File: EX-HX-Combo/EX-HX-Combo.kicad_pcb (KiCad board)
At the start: 2 copper layers, 150.2 x 124.5 mm, 40 parts, among them CN1 DB9 Male, J1 IDE_CONNECTOR, J200 Bus_Tandy_Plus_Through, J3 Bus_Tandy_Plus, SW1 SW_DIP_x10, U1 BIOS FLASH, U2 74HCT245, U3 1.8432 MHz, U4 DS1315, U5 AS6C4008-55PCN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

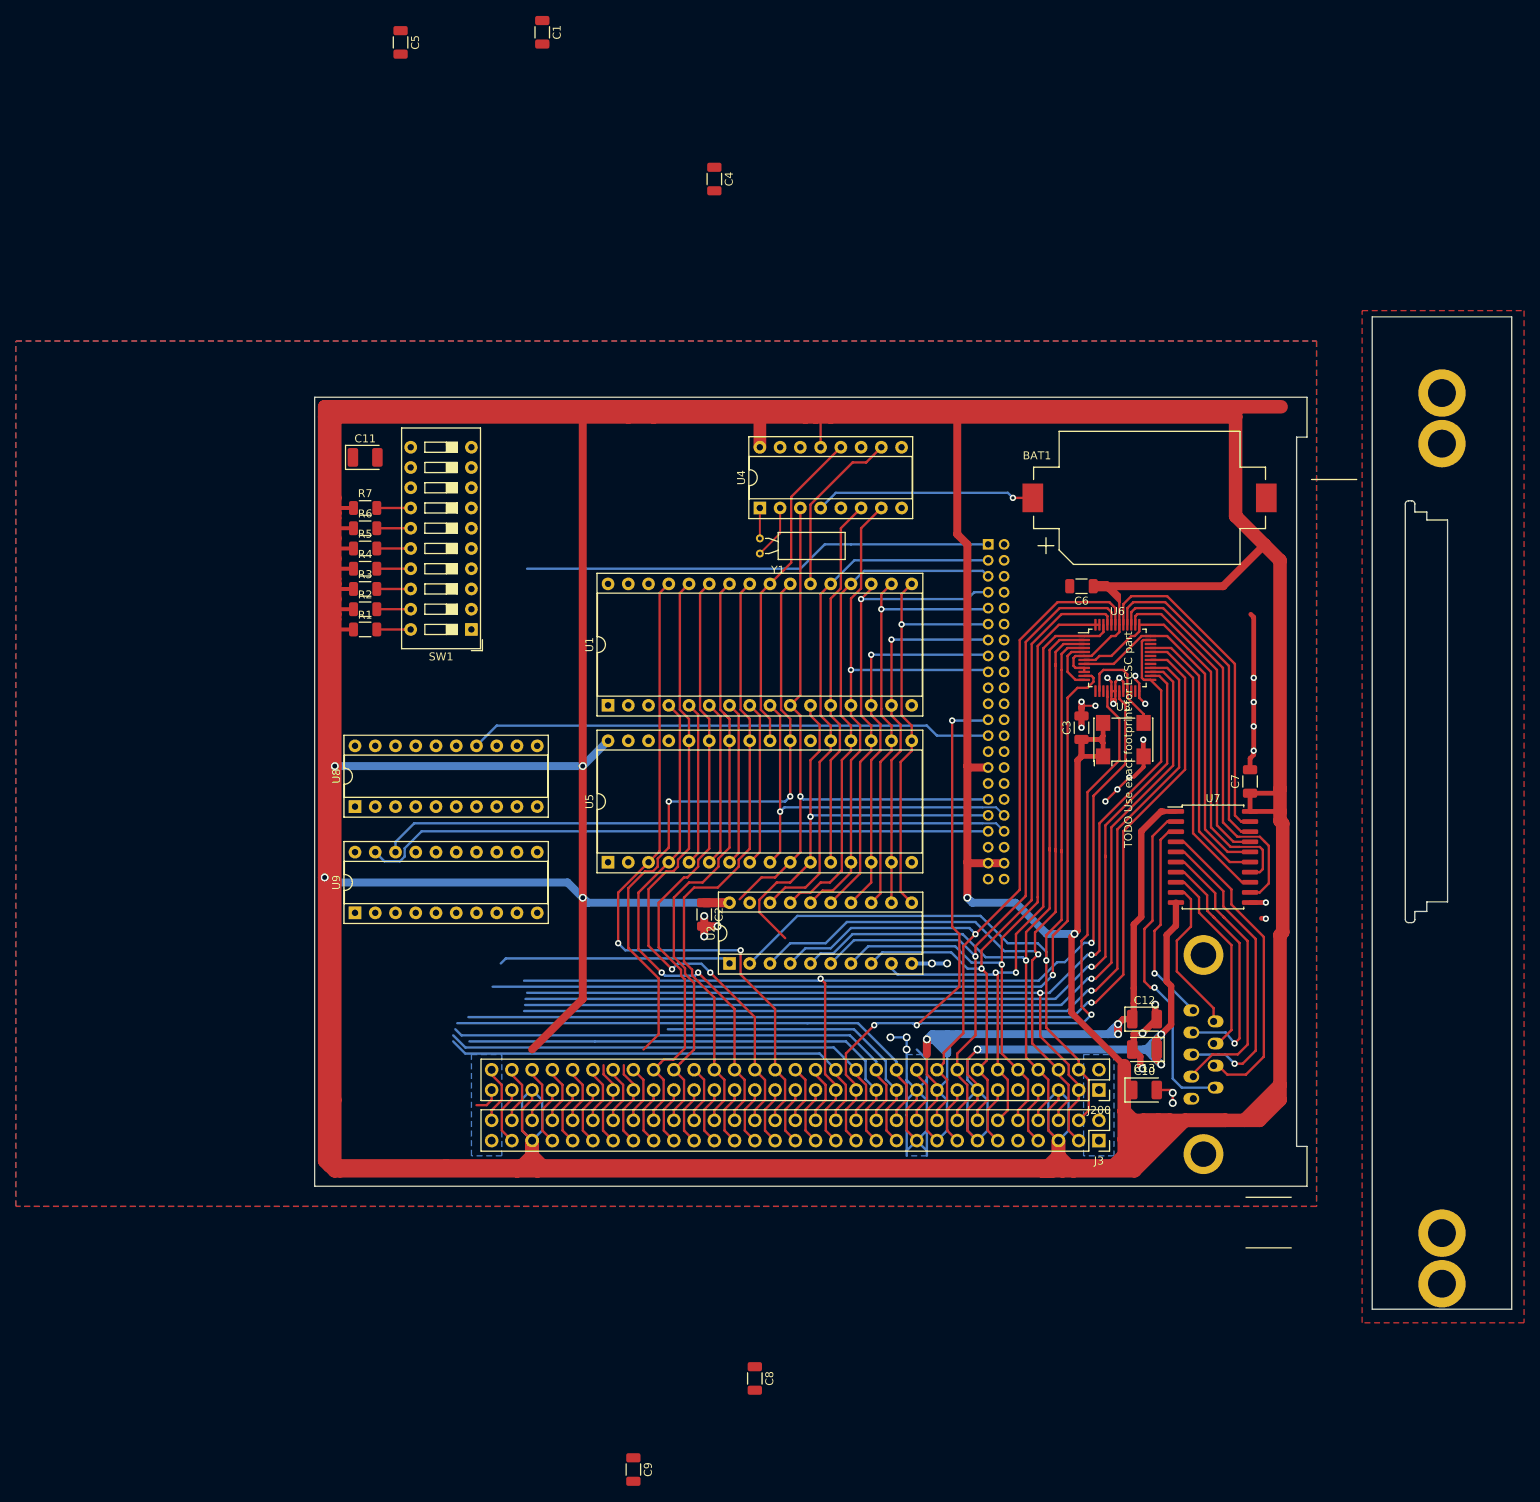
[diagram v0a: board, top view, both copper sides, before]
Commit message: More layout work on EX-HX combo.
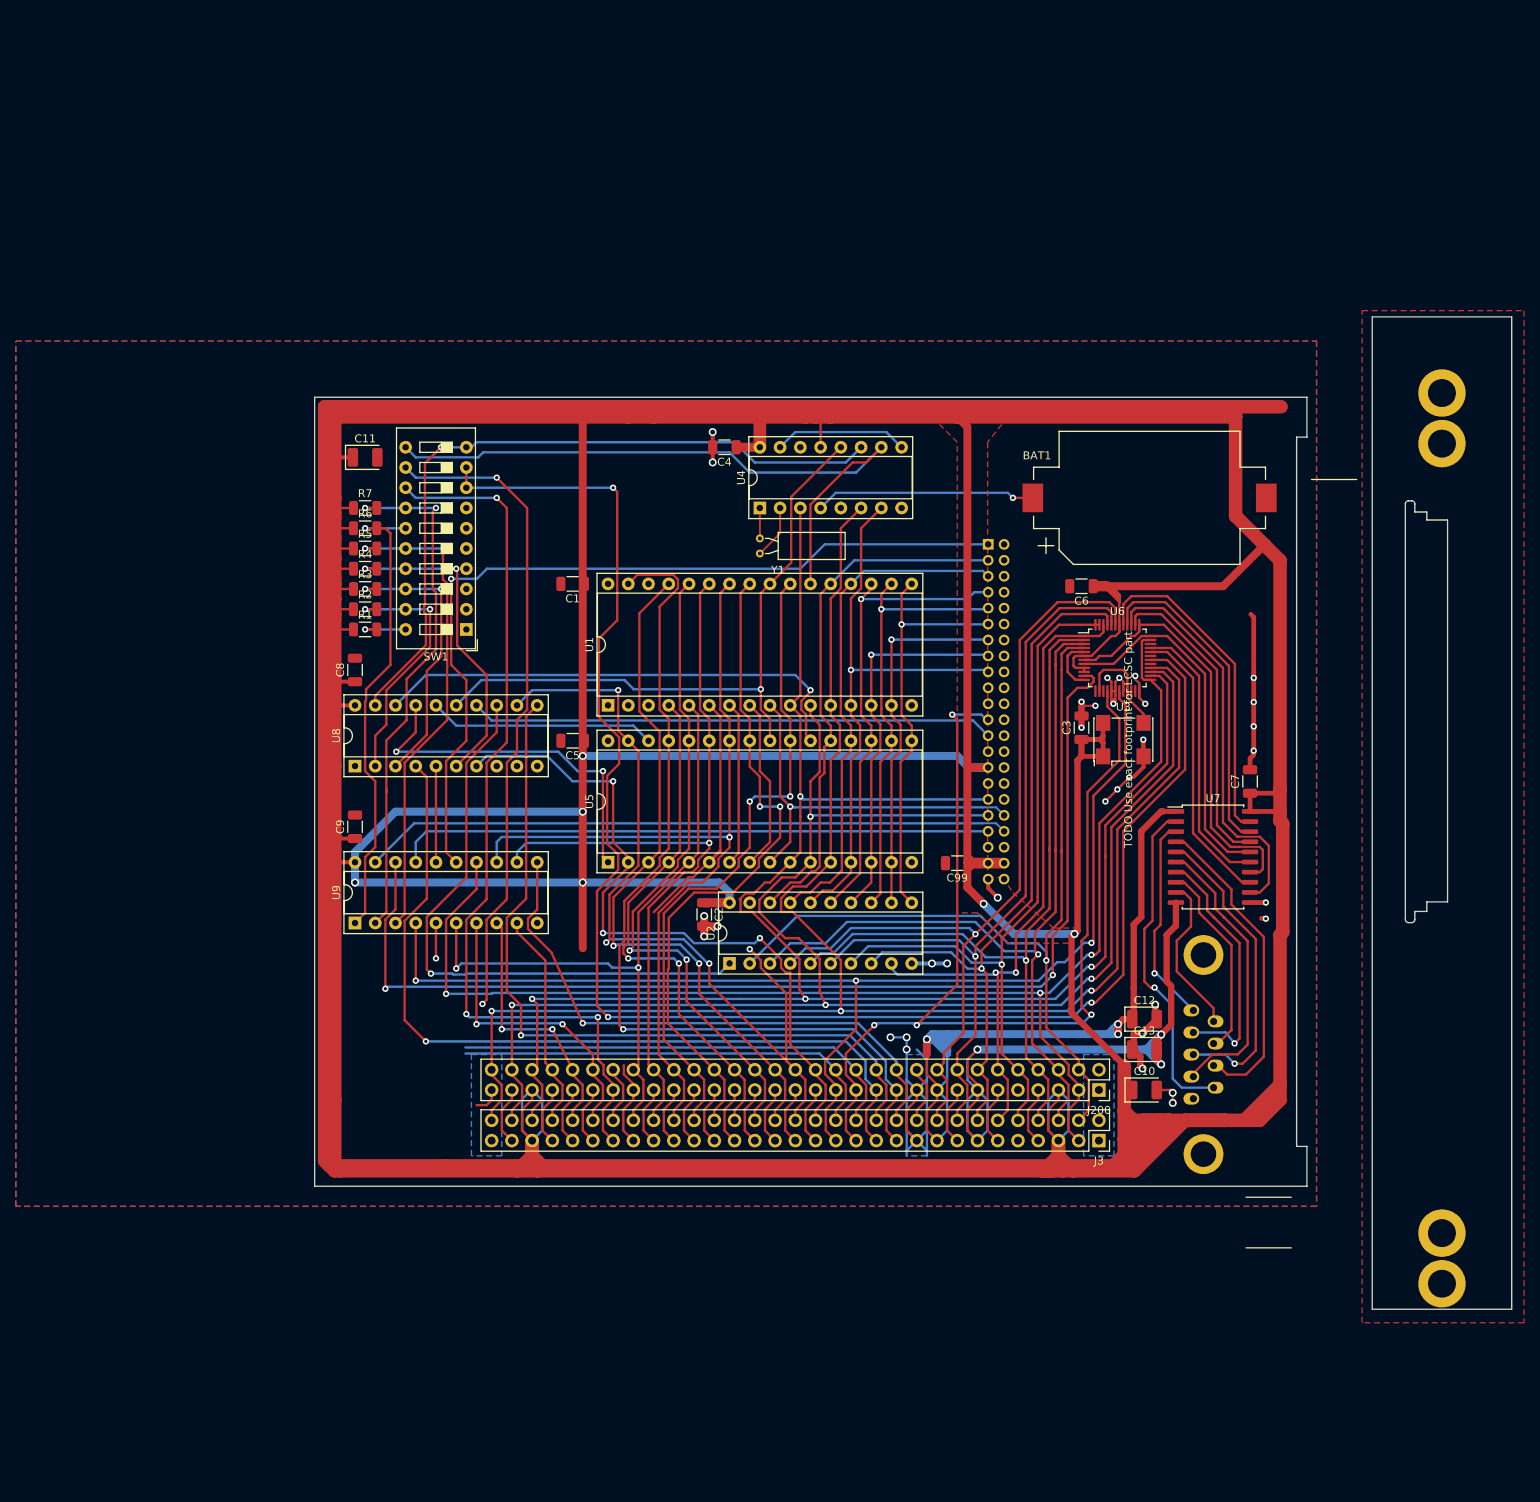
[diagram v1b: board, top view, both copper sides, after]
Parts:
- added C99: 0.1uF, Capacitor_SMD:C_1206_3216Metric, F.Cu at (200.7, 96.0)
- moved C8 102.1 mm to (125.1, 71.8), turned to 90 degrees
- moved C5 90.3 mm to (152.4, 80.6), turned to 180 degrees
- moved C9 87.9 mm to (125.1, 91.4), turned to 90 degrees
- moved C1 69.3 mm to (152.4, 61.0), turned to 180 degrees
- moved C4 33.7 mm to (171.4, 43.8), turned to 180 degrees
- moved U8 5.08 mm to (125.1, 83.8)
- moved U9 1.27 mm to (125.1, 103.5)
- moved SW1 0.63 mm to (139.1, 66.7)
- turned C13 to 0 degrees
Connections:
- SW1 pad 10: ~CE~_BIOS_THRU -> ~CE~_BIOS_DECODE
- SW1 pad 11: ~CE~_BIOS_DECODE -> ~CE~_BIOS_THRU
- U9 pad 1: UART_S1 -> UART_S0
- U9 pad 17: ~UART_CS -> ~CS1~_ATA
- U9 pad 18: ~CS3~_ATA -> ~UART_CS
- U9 pad 19: ~CS1~_ATA -> ~CS3~_ATA
- U9 pad 2: UART_S0 -> UART_S1
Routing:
- net IRQ3: track 11.0 -> 113.4 mm, vias 0 -> 3
- net A15: track 7.39 -> 104.9 mm, vias 0 -> 4
- net ~CE~_BIOS_DECODE: track 0.00 -> 90.8 mm, vias 0 -> 1
- net IRQ4: track 11.0 -> 92.9 mm, vias 0 -> 2
- net A16: track 7.39 -> 87.7 mm, vias 0 -> 3
- net UART_IRQ: track 130.1 -> 204.4 mm, vias 1 -> 3
- net ~MEMW: track 40.6 -> 113.8 mm, vias 0 -> 1
- net ~CE~_BIOS_THRU: track 21.8 -> 84.7 mm
- net UART_S1: track 4.25 -> 66.4 mm, vias 0 -> 2
- net ~CE~_RAM_DECODE: track 0.00 -> 61.7 mm, vias 0 -> 1
- net A07: track 28.0 -> 86.1 mm, vias 0 -> 2
- net ATA_ADDR_JUMPER: track 4.25 -> 61.7 mm, vias 0 -> 2
- net UART_S0: track 4.25 -> 60.8 mm, vias 0 -> 1
- net ~RESET: track 59.1 -> 107.1 mm, vias 0 -> 1
- net A18_MAPPED: track 0.00 -> 47.3 mm, vias 0 -> 2
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- added copper zone on F.Cu, net VCC

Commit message: WIP on EX-HX-Combo layout - left side of board.
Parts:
- moved SW1 0.63 mm to (139.7, 66.7)
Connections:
- U8 pad 11: A19 -> A15
- U8 pad 12: A15 -> UMB_SIZE
- U8 pad 13: ~BUFF_READ -> ~IOR~_DELAYED
- U8 pad 14: ~IOR~_DELAYED -> ~MEMR~_DELAYED
- U8 pad 15: ~MEMR~_DELAYED -> A17_MAPPED
- U8 pad 16: A17_MAPPED -> ~BUFF_READ
- U8 pad 3: UMB_ENABLE -> ~MEMR
- U8 pad 4: ~MEMR -> IOR_DECODE
- U8 pad 5: IOR_DECODE -> UMB_ENABLE
- U8 pad 6: UMB_SIZE -> A16
- U8 pad 7: A16 -> A17
- U8 pad 8: A17 -> A18
- U8 pad 9: A18 -> A19
- U9 pad 11: AEN -> A07
- U9 pad 12: A08 -> A06
- U9 pad 13: A09 -> A08
- U9 pad 14: RESET -> A09
- U9 pad 15: ~RESET -> ~CS1~_ATA
- U9 pad 16: IOR_DECODE -> ~RESET
- U9 pad 17: ~CS1~_ATA -> IOR_DECODE
- U9 pad 18: ~UART_CS -> ~CS3~_ATA
- U9 pad 19: ~CS3~_ATA -> ~UART_CS
- U9 pad 3: ATA_ADDR_JUMPER -> ~IOR
- U9 pad 4: ~IOR -> RESET
- U9 pad 5: A06 -> A03
- U9 pad 6: A07 -> A04
- U9 pad 7: A05 -> ATA_ADDR_JUMPER
- U9 pad 8: A04 -> A05
- U9 pad 9: A03 -> AEN
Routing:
- net A17: track 54.7 -> 83.3 mm, vias 0 -> 1
- net A18: track 57.6 -> 85.1 mm, vias 0 -> 1
- net A06: track 44.4 -> 65.5 mm, vias 1 -> 0
- net BASE_RAM_ENABLE: track 7.18 -> 25.5 mm
- net A19: track 98.1 -> 85.7 mm
- net IRQ4: track 92.9 -> 104.7 mm, vias 2 -> 1
- net A02: track 226.0 -> 236.2 mm
- net A07: track 86.1 -> 77.0 mm, vias 2 -> 0
- net ATA_ADDR_JUMPER: track 61.7 -> 69.6 mm
- net A05: track 58.9 -> 51.4 mm, vias 2 -> 0
- net AEN: track 72.5 -> 65.9 mm
- net ~CS1~_ATA: track 74.9 -> 68.4 mm
- net A00: track 212.3 -> 218.6 mm
- net RESET: track 168.6 -> 163.2 mm
- net ~CE~_BIOS_DECODE: track 90.8 -> 95.9 mm, vias 1 -> 0
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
